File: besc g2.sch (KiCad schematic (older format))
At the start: 9 parts

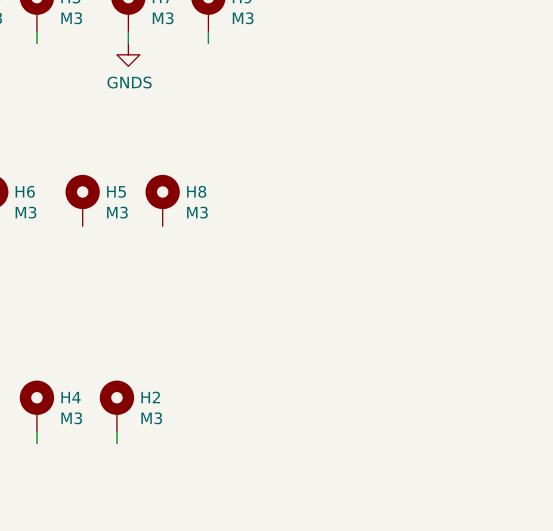
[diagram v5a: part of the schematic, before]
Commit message: finished routing, added bom and step
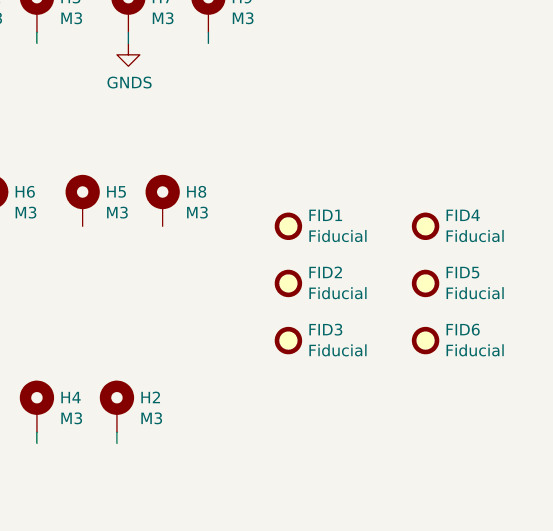
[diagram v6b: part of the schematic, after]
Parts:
- added FID1, FID2, FID3, FID4, FID5, FID6: Fiducial, Fiducial:Fiducial_0.5mm_Mask1.5mm, symbol Mechanical:Fiducial
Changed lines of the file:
@@
 encoding utf-8
 Sheet 1 5
-Title ""
-Date "2019-03-28"
+Title "BESC Gen 2"
+Date "14.7.2019"
 Rev "init"
-Comp ""
+Comp "e.pavlin.si"
 Comment1 ""
 Comment2 ""
@@
 	8450 2150 8750 2150
 Connection ~ 8750 2150
+$Comp
+L Mechanical:Fiducial FID1
+U 1 1 5D6CCC37
+P 9800 3800
+F 0 "FID1" H 9885 3846 50  0000 L CNN
+F 1 "Fiducial" H 9885 3755 50  0000 L CNN
+F 2 "Fiducial:Fiducial_0.5mm_Mask1.5mm" H 9800 3800 50  0001 C CNN
+F 3 "~" H 9800 3800 50  0001 C CNN
+	1    9800 3800
+	1    0    0    -1
+$EndComp
+$Comp
+L Mechanical:Fiducial FID2
+U 1 1 5D6CD10F
+P 9800 4050
+F 0 "FID2" H 9885 4096 50  0000 L CNN
+F 1 "Fiducial" H 9885 4005 50  0000 L CNN
+F 2 "Fiducial:Fiducial_0.5mm_Mask1.5mm" H 9800 4050 50  0001 C CNN
+F 3 "~" H 9800 4050 50  0001 C CNN
+	1    9800 4050
+	1    0    0    -1
+$EndComp
+$Comp
+L Mechanical:Fiducial FID3
+U 1 1 5D6CD3DE
+P 9800 4300
+F 0 "FID3" H 9885 4346 50  0000 L CNN
+F 1 "Fiducial" H 9885 4255 50  0000 L CNN
+F 2 "Fiducial:Fiducial_0.5mm_Mask1.5mm" H 9800 4300 50  0001 C CNN
+F 3 "~" H 9800 4300 50  0001 C CNN
+	1    9800 4300
+	1    0    0    -1
+$EndComp
+$Comp
+L Mechanical:Fiducial FID4
+U 1 1 5D6CF19D
+P 10400 3800
+F 0 "FID4" H 10485 3846 50  0000 L CNN
+F 1 "Fiducial" H 10485 3755 50  0000 L CNN
+F 2 "Fiducial:Fiducial_0.5mm_Mask1.5mm" H 10400 3800 50  0001 C CNN
+F 3 "~" H 10400 3800 50  0001 C CNN
+	1    10400 3800
+	1    0    0    -1
+$EndComp
+$Comp
+L Mechanical:Fiducial FID5
+U 1 1 5D6CF1A3
+P 10400 4050
+F 0 "FID5" H 10485 4096 50  0000 L CNN
+F 1 "Fiducial" H 10485 4005 50  0000 L CNN
+F 2 "Fiducial:Fiducial_0.5mm_Mask1.5mm" H 10400 4050 50  0001 C CNN
+F 3 "~" H 10400 4050 50  0001 C CNN
+	1    10400 4050
+	1    0    0    -1
+$EndComp
+$Comp
+L Mechanical:Fiducial FID6
+U 1 1 5D6CF1A9
+P 10400 4300
+F 0 "FID6" H 10485 4346 50  0000 L CNN
+F 1 "Fiducial" H 10485 4255 50  0000 L CNN
+F 2 "Fiducial:Fiducial_0.5mm_Mask1.5mm" H 10400 4300 50  0001 C CNN
+F 3 "~" H 10400 4300 50  0001 C CNN
+	1    10400 4300
+	1    0    0    -1
+$EndComp
 $EndSCHEMATC
